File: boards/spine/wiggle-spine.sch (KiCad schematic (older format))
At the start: 0 parts

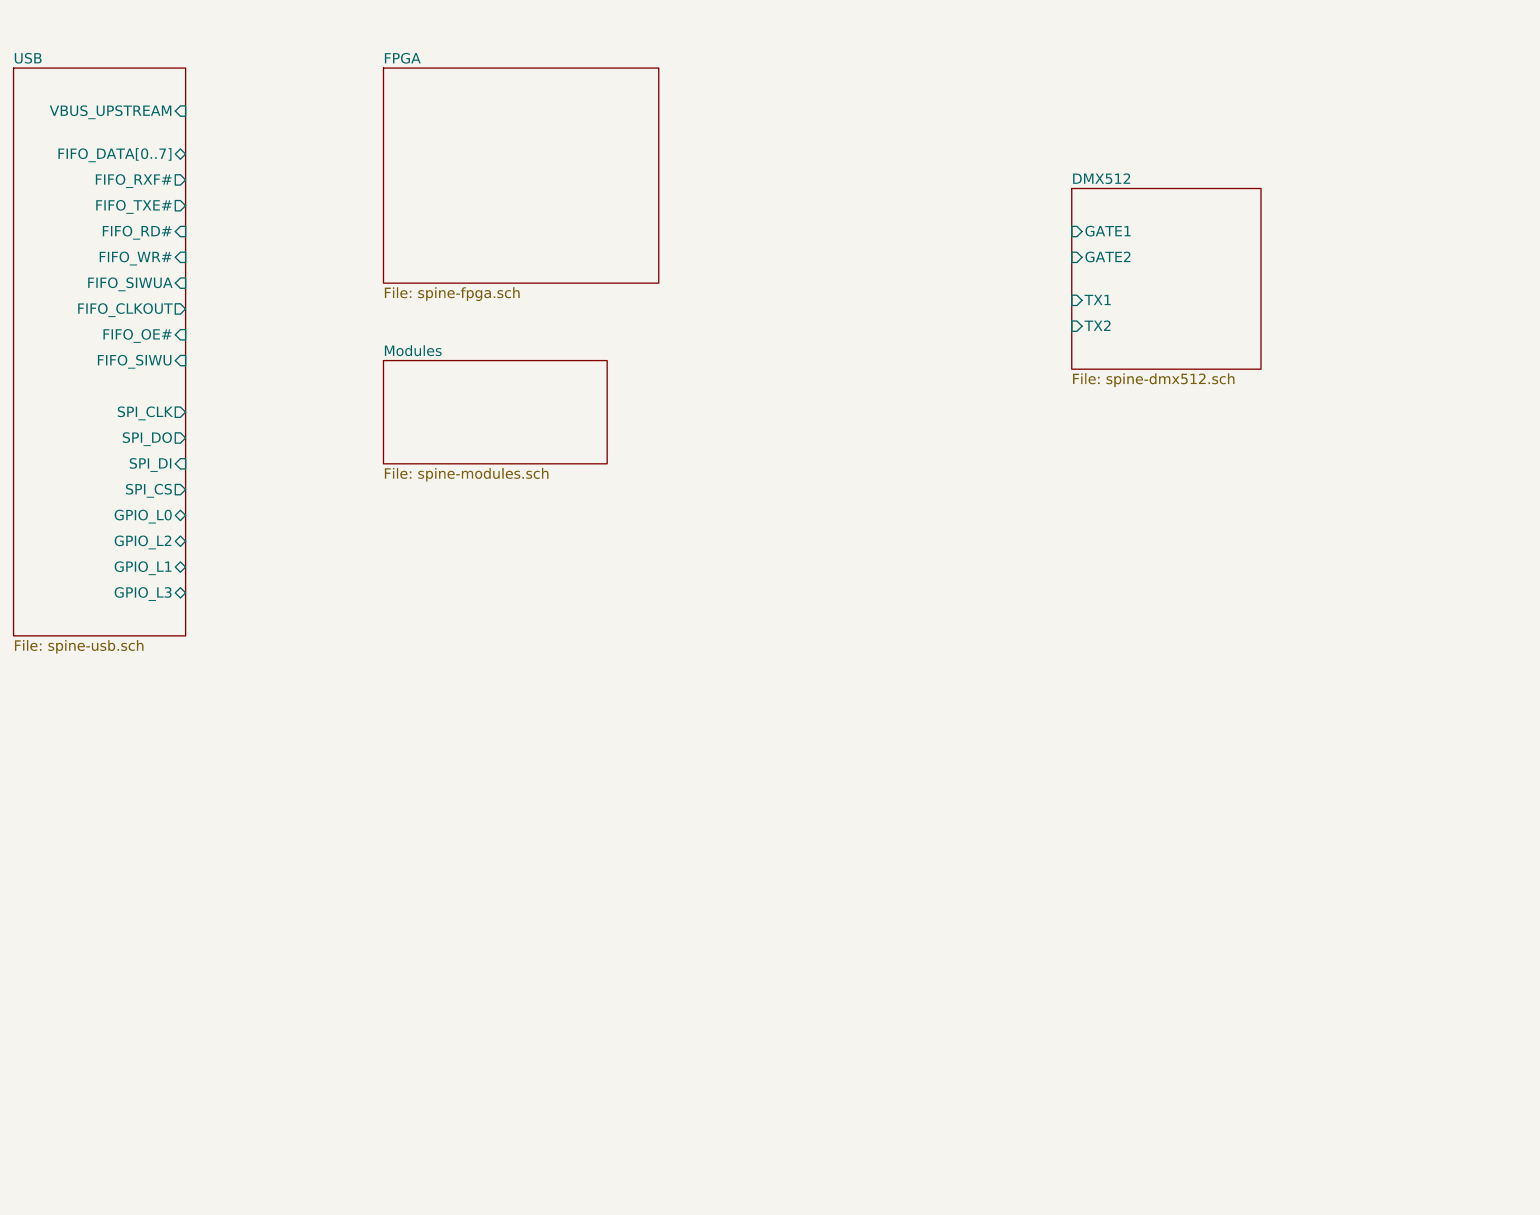
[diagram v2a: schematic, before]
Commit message: Getting the FPGA set up
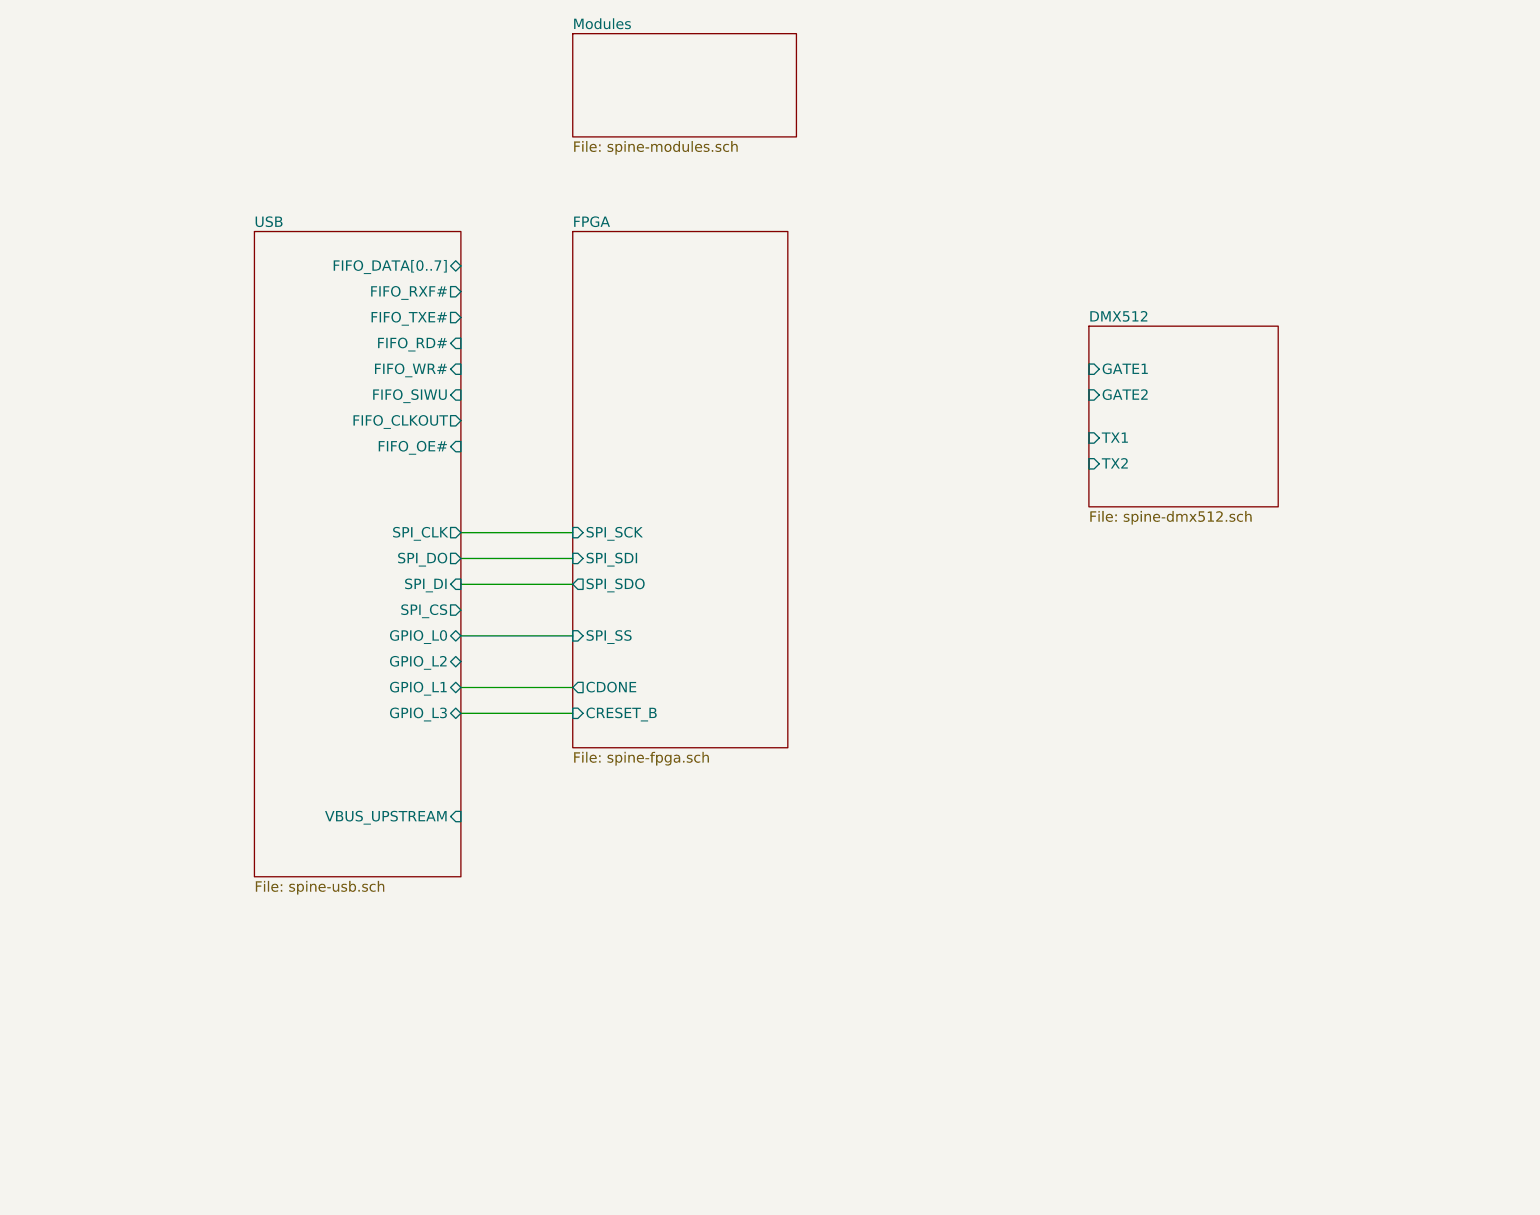
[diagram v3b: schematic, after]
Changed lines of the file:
@@
 $EndDescr
 $Sheet
-S 1250 1350 1000 3300
+S 2650 2300 1200 3750
 U 5637B4E6
 F0 "USB" 60
 F1 "spine-usb.sch" 60
-F2 "FIFO_DATA[0..7]" B R 2250 1850 60
-F3 "VBUS_UPSTREAM" I R 2250 1600 60
-F4 "FIFO_RXF#" O R 2250 2000 60
-F5 "FIFO_TXE#" O R 2250 2150 60
-F6 "FIFO_RD#" I R 2250 2300 60
-F7 "FIFO_WR#" I R 2250 2450 60
-F8 "FIFO_SIWUA" I R 2250 2600 60
-F9 "FIFO_CLKOUT" O R 2250 2750 60
-F10 "FIFO_OE#" I R 2250 2900 60
-F11 "FIFO_SIWU" I R 2250 3050 60
-F12 "SPI_CLK" O R 2250 3350 60
-F13 "SPI_DO" O R 2250 3500 60
-F14 "SPI_DI" I R 2250 3650 60
-F15 "SPI_CS" O R 2250 3800 60
-F16 "GPIO_L0" B R 2250 3950 60
-F17 "GPIO_L2" B R 2250 4100 60
-F18 "GPIO_L1" B R 2250 4250 60
-F19 "GPIO_L3" B R 2250 4400 60
+F2 "FIFO_DATA[0..7]" B R 3850 2500 60
+F3 "VBUS_UPSTREAM" I R 3850 5700 60
+F4 "FIFO_RXF#" O R 3850 2650 60
+F5 "FIFO_TXE#" O R 3850 2800 60
+F6 "FIFO_RD#" I R 3850 2950 60
+F7 "FIFO_WR#" I R 3850 3100 60
+F8 "FIFO_SIWU" I R 3850 3250 60
+F9 "FIFO_CLKOUT" O R 3850 3400 60
+F10 "FIFO_OE#" I R 3850 3550 60
+F11 "SPI_CLK" O R 3850 4050 60
+F12 "SPI_DO" O R 3850 4200 60
+F13 "SPI_DI" I R 3850 4350 60
+F14 "SPI_CS" O R 3850 4500 60
+F15 "GPIO_L0" B R 3850 4650 60
+F16 "GPIO_L2" B R 3850 4800 60
+F17 "GPIO_L1" B R 3850 4950 60
+F18 "GPIO_L3" B R 3850 5100 60
 $EndSheet
 $Sheet
-S 3400 1350 1600 1250
+S 4500 2300 1250 3000
 U 5637E2EA
 F0 "FPGA" 60
 F1 "spine-fpga.sch" 60
+F2 "SPI_SDO" O L 4500 4350 60
+F3 "SPI_SDI" I L 4500 4200 60
+F4 "SPI_SCK" I L 4500 4050 60
+F5 "SPI_SS" I L 4500 4650 60
+F6 "CDONE" O L 4500 4950 60
+F7 "CRESET_B" I L 4500 5100 60
 $EndSheet
 $Sheet
-S 7400 2050 1100 1050
+S 7500 2850 1100 1050
 U 563E737A
 F0 "DMX512" 60
 F1 "spine-dmx512.sch" 60
-F2 "GATE1" I L 7400 2300 60
-F3 "GATE2" I L 7400 2450 60
-F4 "TX1" I L 7400 2700 60
-F5 "TX2" I L 7400 2850 60
+F2 "GATE1" I L 7500 3100 60
+F3 "GATE2" I L 7500 3250 60
+F4 "TX1" I L 7500 3500 60
+F5 "TX2" I L 7500 3650 60
 $EndSheet
 $Sheet
-S 3400 3050 1300 600
+S 4500 1150 1300 600
 U 5641D2D7
 F0 "Modules" 60
 F1 "spine-modules.sch" 60
 $EndSheet
+Wire Wire Line
+	3850 4650 4500 4650
+Wire Wire Line
+	4500 5100 3850 5100
+Wire Wire Line
+	3850 4050 4500 4050
+Wire Wire Line
+	4500 4200 3850 4200
+Wire Wire Line
+	3850 4350 4500 4350
+Wire Wire Line
+	3850 4950 4500 4950
 $EndSCHEMATC

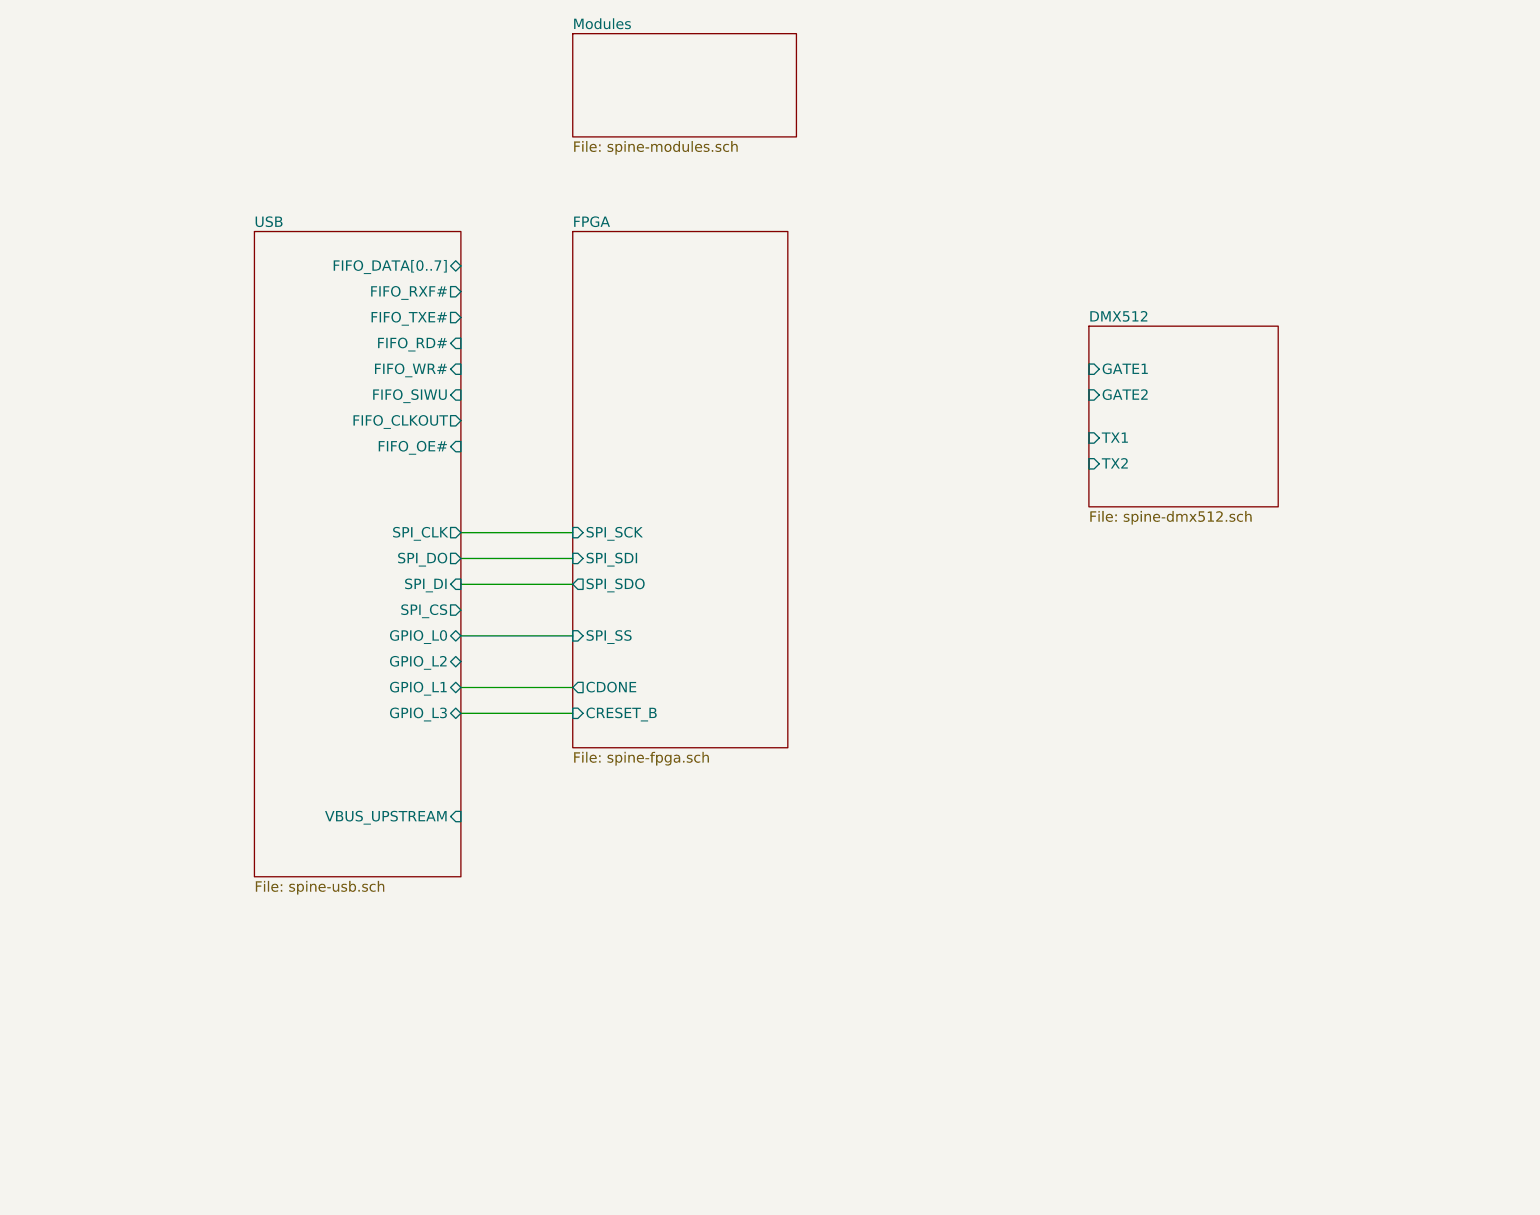
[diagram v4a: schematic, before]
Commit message: Early power management work
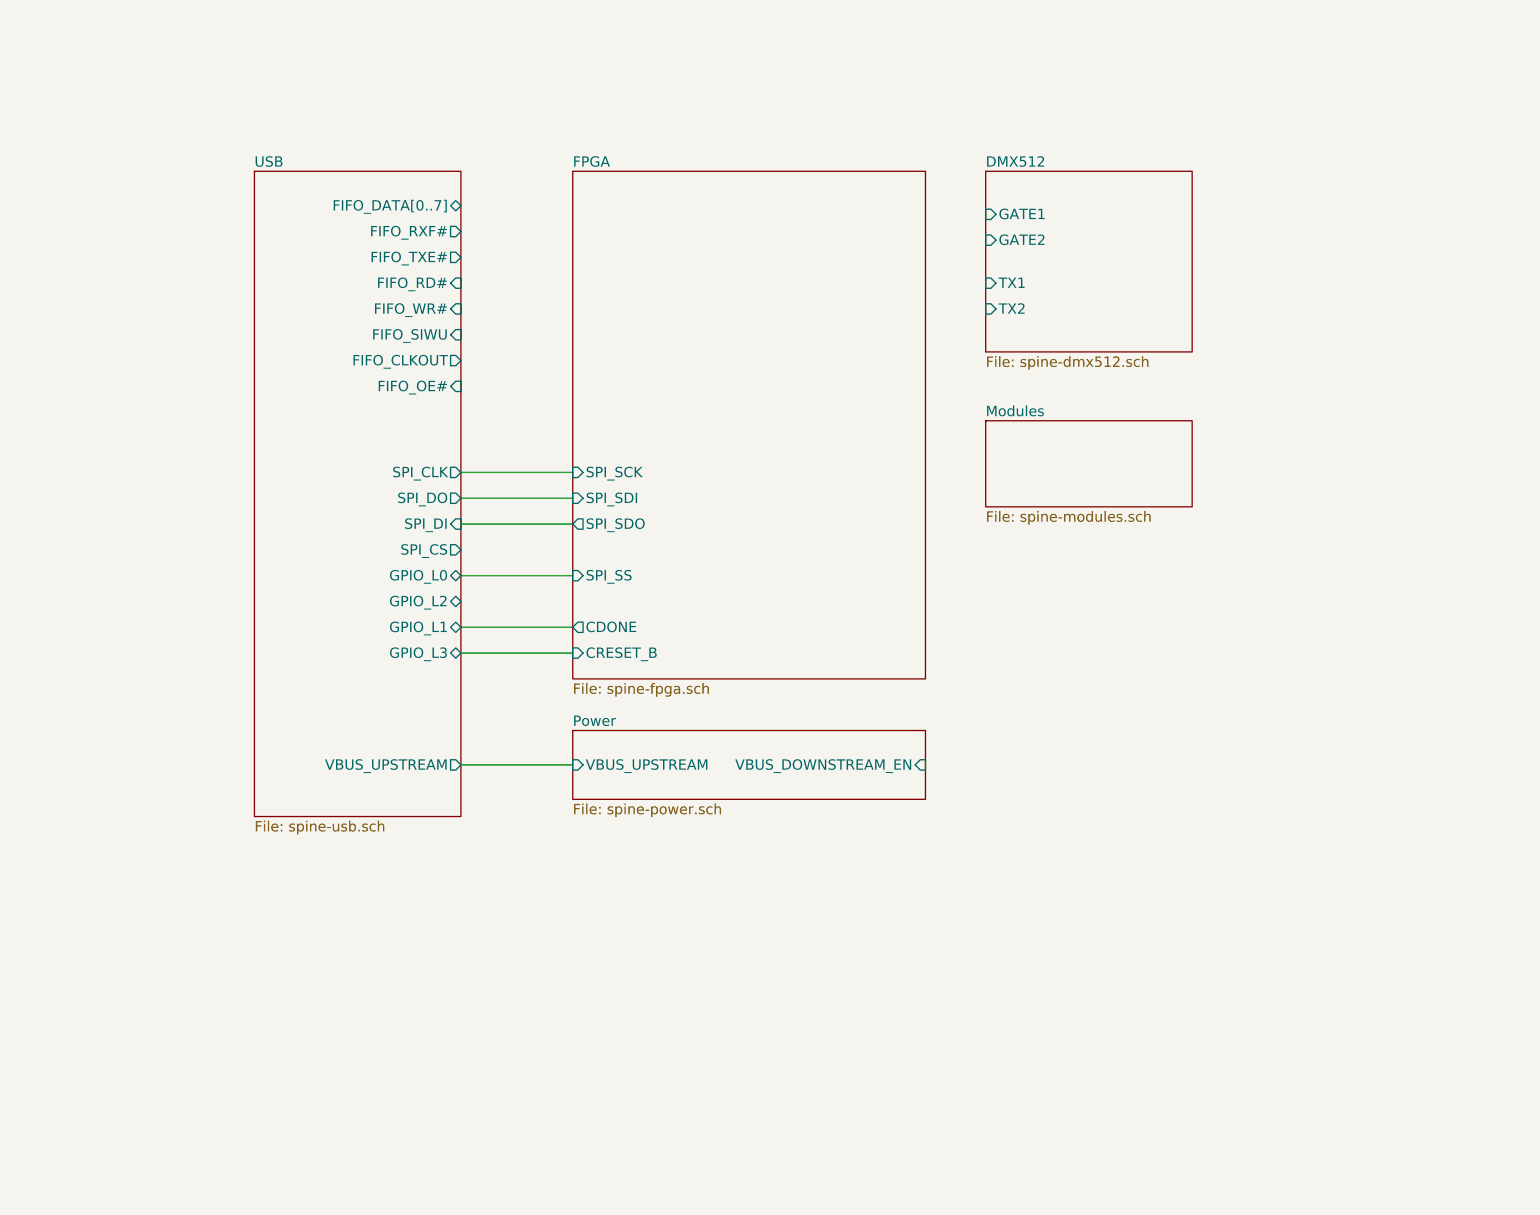
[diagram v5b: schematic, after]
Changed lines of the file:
@@
 $Descr USLetter 11000 8500
 encoding utf-8
-Sheet 1 5
+Sheet 1 6
 Title ""
 Date ""
@@
 $EndDescr
 $Sheet
-S 2650 2300 1200 3750
+S 2650 1950 1200 3750
 U 5637B4E6
 F0 "USB" 60
 F1 "spine-usb.sch" 60
-F2 "FIFO_DATA[0..7]" B R 3850 2500 60
-F3 "VBUS_UPSTREAM" I R 3850 5700 60
-F4 "FIFO_RXF#" O R 3850 2650 60
-F5 "FIFO_TXE#" O R 3850 2800 60
-F6 "FIFO_RD#" I R 3850 2950 60
-F7 "FIFO_WR#" I R 3850 3100 60
-F8 "FIFO_SIWU" I R 3850 3250 60
-F9 "FIFO_CLKOUT" O R 3850 3400 60
-F10 "FIFO_OE#" I R 3850 3550 60
-F11 "SPI_CLK" O R 3850 4050 60
-F12 "SPI_DO" O R 3850 4200 60
-F13 "SPI_DI" I R 3850 4350 60
-F14 "SPI_CS" O R 3850 4500 60
-F15 "GPIO_L0" B R 3850 4650 60
-F16 "GPIO_L2" B R 3850 4800 60
-F17 "GPIO_L1" B R 3850 4950 60
-F18 "GPIO_L3" B R 3850 5100 60
+F2 "FIFO_DATA[0..7]" B R 3850 2150 60
+F3 "VBUS_UPSTREAM" O R 3850 5400 60
+F4 "FIFO_RXF#" O R 3850 2300 60
+F5 "FIFO_TXE#" O R 3850 2450 60
+F6 "FIFO_RD#" I R 3850 2600 60
+F7 "FIFO_WR#" I R 3850 2750 60
+F8 "FIFO_SIWU" I R 3850 2900 60
+F9 "FIFO_CLKOUT" O R 3850 3050 60
+F10 "FIFO_OE#" I R 3850 3200 60
+F11 "SPI_CLK" O R 3850 3700 60
+F12 "SPI_DO" O R 3850 3850 60
+F13 "SPI_DI" I R 3850 4000 60
+F14 "SPI_CS" O R 3850 4150 60
+F15 "GPIO_L0" B R 3850 4300 60
+F16 "GPIO_L2" B R 3850 4450 60
+F17 "GPIO_L1" B R 3850 4600 60
+F18 "GPIO_L3" B R 3850 4750 60
 $EndSheet
 $Sheet
-S 7500 2850 1100 1050
+S 6900 1950 1200 1050
 U 563E737A
 F0 "DMX512" 60
 F1 "spine-dmx512.sch" 60
-F2 "GATE1" I L 7500 3100 60
-F3 "GATE2" I L 7500 3250 60
-F4 "TX1" I L 7500 3500 60
-F5 "TX2" I L 7500 3650 60
+F2 "GATE1" I L 6900 2200 60
+F3 "GATE2" I L 6900 2350 60
+F4 "TX1" I L 6900 2600 60
+F5 "TX2" I L 6900 2750 60
 $EndSheet
 $Sheet
-S 4500 1150 1300 600
+S 6900 3400 1200 500
 U 5641D2D7
 F0 "Modules" 60
@@
 $EndSheet
 Wire Wire Line
-	3850 4650 4500 4650
+	3850 4300 4500 4300
 Wire Wire Line
-	4500 5100 3850 5100
+	4500 4750 3850 4750
 Wire Wire Line
-	3850 4050 4500 4050
+	3850 3700 4500 3700
 Wire Wire Line
-	4500 4200 3850 4200
+	4500 3850 3850 3850
 Wire Wire Line
-	3850 4350 4500 4350
+	3850 4000 4500 4000
 Wire Wire Line
-	3850 4950 4500 4950
+	3850 4600 4500 4600
 $Sheet
-S 4500 2300 1250 3000
+S 4500 1950 2050 2950
 U 5637E2EA
 F0 "FPGA" 60
 F1 "spine-fpga.sch" 60
-F2 "SPI_SDO" O L 4500 4350 60
-F3 "SPI_SDI" I L 4500 4200 60
-F4 "SPI_SCK" I L 4500 4050 60
-F5 "SPI_SS" I L 4500 4650 60
-F6 "CDONE" O L 4500 4950 60
-F7 "CRESET_B" I L 4500 5100 60
+F2 "SPI_SDO" O L 4500 4000 60
+F3 "SPI_SDI" I L 4500 3850 60
+F4 "SPI_SCK" I L 4500 3700 60
+F5 "SPI_SS" I L 4500 4300 60
+F6 "CDONE" O L 4500 4600 60
+F7 "CRESET_B" I L 4500 4750 60
 $EndSheet
+$Sheet
+S 4500 5200 2050 400
+U 5642944E
+F0 "Power" 60
+F1 "spine-power.sch" 60
+F2 "VBUS_UPSTREAM" I L 4500 5400 60
+F3 "VBUS_DOWNSTREAM_EN" I R 6550 5400 60
+$EndSheet
+Wire Wire Line
+	3850 5400 4500 5400
 $EndSCHEMATC

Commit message: Power management and such
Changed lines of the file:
@@
 F6 "CDONE" O L 4500 4600 60
 F7 "CRESET_B" I L 4500 4750 60
+F8 "FIFO_DATA[0..7]" B L 4500 2150 60
+F9 "FIFO_RXF#" I L 4500 2300 60
+F10 "FIFO_TXE#" I L 4500 2450 60
+F11 "FIFO_RD#" O L 4500 2600 60
+F12 "FIFO_WR#" O L 4500 2750 60
+F13 "FIFO_SIWU" O L 4500 2900 60
+F14 "FIFO_CLKOUT" I L 4500 3050 60
+F15 "FIFO_OE#" O L 4500 3200 60
+F16 "DMX_GATE1" O R 6550 2200 60
+F17 "DMX_GATE2" O R 6550 2350 60
+F18 "DMX_TX1" O R 6550 2600 60
+F19 "DMX_TX2" O R 6550 2750 60
+F20 "VBUS_DOWNSTREAM_EN" O R 6550 4700 60
 $EndSheet
 $Sheet
@@
 Wire Wire Line
 	3850 5400 4500 5400
+Wire Bus Line
+	3850 2150 4500 2150
+Wire Wire Line
+	3850 2300 4500 2300
+Wire Wire Line
+	4500 2450 3850 2450
+Wire Wire Line
+	3850 2600 4500 2600
+Wire Wire Line
+	3850 2750 4500 2750
+Wire Wire Line
+	4500 2900 3850 2900
+Wire Wire Line
+	3850 3050 4500 3050
+Wire Wire Line
+	4500 3200 3850 3200
+Wire Wire Line
+	6550 2200 6900 2200
+Wire Wire Line
+	6900 2350 6550 2350
+Wire Wire Line
+	6550 2600 6900 2600
+Wire Wire Line
+	6550 2750 6900 2750
+Wire Wire Line
+	6550 4700 6850 4700
+Wire Wire Line
+	6850 4700 6850 5400
+Wire Wire Line
+	6850 5400 6550 5400
 $EndSCHEMATC
